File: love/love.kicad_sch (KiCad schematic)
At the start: 73 parts, among them U2 Raspberry_Pi_Pico

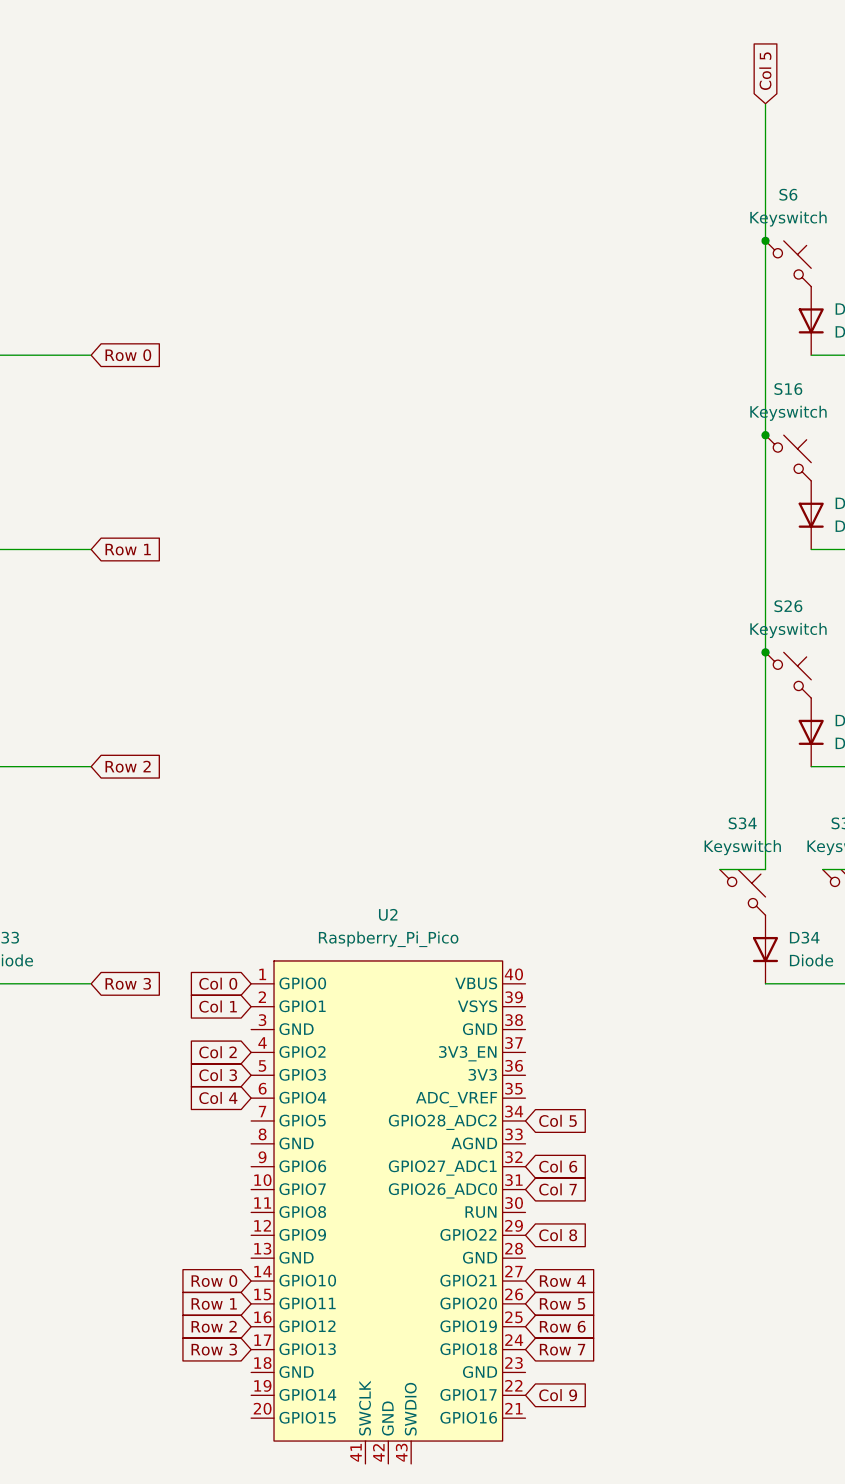
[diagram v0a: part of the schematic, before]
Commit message: adding the traditional 84 key but for somereason i named it 104
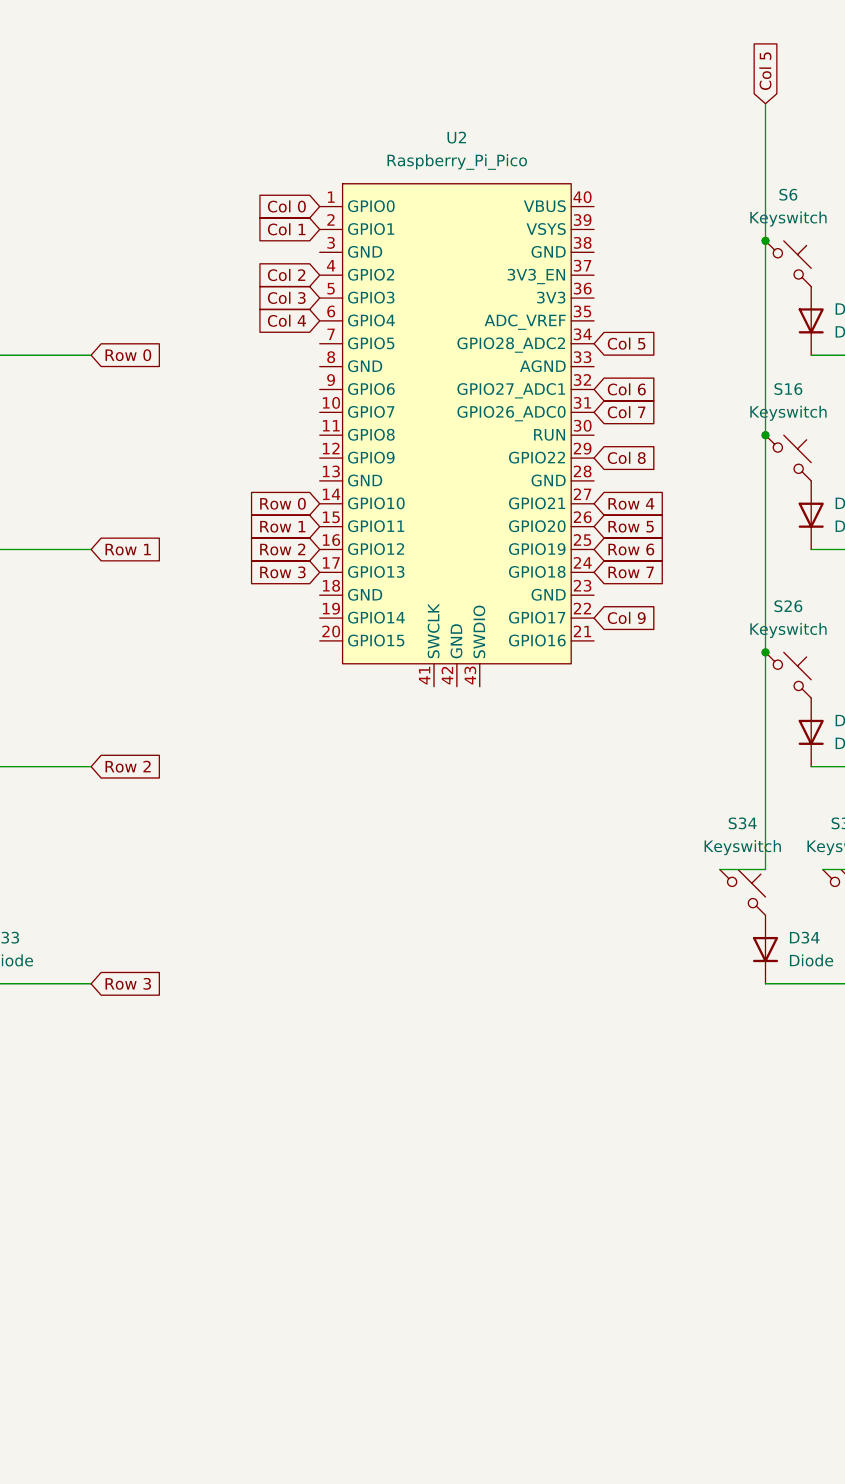
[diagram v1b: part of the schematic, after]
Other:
- moved on the sheet: U2
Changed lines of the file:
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@@
     (stroke (width 0) (type default))
   )
-  (global_label "Col 0" (shape input) (at 127 137.16 180) (fields_autoplaced)
+  (global_label "Col 0" (shape input) (at 134.62 50.8 180) (fields_autoplaced)
     (effects (font (size 1.27 1.27)) (justify right))
-    (property "Intersheetrefs" "${INTERSHEET_REFS}" (at 118.7535 137.16 0)
+    (property "Intersheetrefs" "${INTERSHEET_REFS}" (at 126.3735 50.8 0)
       (effects (font (size 1.27 1.27)) (justify right) hide)
     )
   )
-  (global_label "Col 4" (shape input) (at 127 149.86 180) (fields_autoplaced)
+  (global_label "Col 4" (shape input) (at 134.62 63.5 180) (fields_autoplaced)
     (effects (font (size 1.27 1.27)) (justify right))
-    (property "Intersheetrefs" "${INTERSHEET_REFS}" (at 118.7535 149.86 0)
+    (property "Intersheetrefs" "${INTERSHEET_REFS}" (at 126.3735 63.5 0)
       (effects (font (size 1.27 1.27)) (justify right) hide)
     )
@@
     )
   )
-  (global_label "Row 5" (shape input) (at 157.48 172.72 0) (fields_autoplaced)
-    (effects (font (size 1.27 1.27)) (justify left))
-    (property "Intersheetrefs" "${INTERSHEET_REFS}" (at 166.3918 172.72 0)
+  (global_label "Row 5" (shape input) (at 165.1 86.36 0) (fields_autoplaced)
+    (effects (font (size 1.27 1.27)) (justify left))
+    (property "Intersheetrefs" "${INTERSHEET_REFS}" (at 174.0118 86.36 0)
       (effects (font (size 1.27 1.27)) (justify left) hide)
     )
@@
     )
   )
-  (global_label "Col 7" (shape input) (at 157.48 160.02 0) (fields_autoplaced)
-    (effects (font (size 1.27 1.27)) (justify left))
-    (property "Intersheetrefs" "${INTERSHEET_REFS}" (at 165.7265 160.02 0)
+  (global_label "Col 7" (shape input) (at 165.1 73.66 0) (fields_autoplaced)
+    (effects (font (size 1.27 1.27)) (justify left))
+    (property "Intersheetrefs" "${INTERSHEET_REFS}" (at 173.3465 73.66 0)
       (effects (font (size 1.27 1.27)) (justify left) hide)
     )
@@
     )
   )
-  (global_label "Col 6" (shape input) (at 157.48 157.48 0) (fields_autoplaced)
-    (effects (font (size 1.27 1.27)) (justify left))
-    (property "Intersheetrefs" "${INTERSHEET_REFS}" (at 165.7265 157.48 0)
-      (effects (font (size 1.27 1.27)) (justify left) hide)
-    )
-  )
-  (global_label "Row 2" (shape input) (at 127 175.26 180) (fields_autoplaced)
+  (global_label "Col 6" (shape input) (at 165.1 71.12 0) (fields_autoplaced)
+    (effects (font (size 1.27 1.27)) (justify left))
+    (property "Intersheetrefs" "${INTERSHEET_REFS}" (at 173.3465 71.12 0)
+      (effects (font (size 1.27 1.27)) (justify left) hide)
+    )
+  )
+  (global_label "Row 2" (shape input) (at 134.62 88.9 180) (fields_autoplaced)
     (effects (font (size 1.27 1.27)) (justify right))
-    (property "Intersheetrefs" "${INTERSHEET_REFS}" (at 118.0882 175.26 0)
+    (property "Intersheetrefs" "${INTERSHEET_REFS}" (at 125.7082 88.9 0)
       (effects (font (size 1.27 1.27)) (justify right) hide)
     )
   )
-  (global_label "Row 3" (shape input) (at 127 177.8 180) (fields_autoplaced)
+  (global_label "Row 3" (shape input) (at 134.62 91.44 180) (fields_autoplaced)
     (effects (font (size 1.27 1.27)) (justify right))
-    (property "Intersheetrefs" "${INTERSHEET_REFS}" (at 118.0882 177.8 0)
+    (property "Intersheetrefs" "${INTERSHEET_REFS}" (at 125.7082 91.44 0)
       (effects (font (size 1.27 1.27)) (justify right) hide)
     )
@@
     )
   )
-  (global_label "Col 5" (shape input) (at 157.48 152.4 0) (fields_autoplaced)
-    (effects (font (size 1.27 1.27)) (justify left))
-    (property "Intersheetrefs" "${INTERSHEET_REFS}" (at 165.7265 152.4 0)
+  (global_label "Col 5" (shape input) (at 165.1 66.04 0) (fields_autoplaced)
+    (effects (font (size 1.27 1.27)) (justify left))
+    (property "Intersheetrefs" "${INTERSHEET_REFS}" (at 173.3465 66.04 0)
       (effects (font (size 1.27 1.27)) (justify left) hide)
     )
@@
     )
   )
-  (global_label "Col 9" (shape input) (at 157.48 182.88 0) (fields_autoplaced)
-    (effects (font (size 1.27 1.27)) (justify left))
-    (property "Intersheetrefs" "${INTERSHEET_REFS}" (at 165.7265 182.88 0)
-      (effects (font (size 1.27 1.27)) (justify left) hide)
-    )
-  )
-  (global_label "Col 3" (shape input) (at 127 147.32 180) (fields_autoplaced)
+  (global_label "Col 9" (shape input) (at 165.1 96.52 0) (fields_autoplaced)
+    (effects (font (size 1.27 1.27)) (justify left))
+    (property "Intersheetrefs" "${INTERSHEET_REFS}" (at 173.3465 96.52 0)
+      (effects (font (size 1.27 1.27)) (justify left) hide)
+    )
+  )
+  (global_label "Col 3" (shape input) (at 134.62 60.96 180) (fields_autoplaced)
     (effects (font (size 1.27 1.27)) (justify right))
-    (property "Intersheetrefs" "${INTERSHEET_REFS}" (at 118.7535 147.32 0)
+    (property "Intersheetrefs" "${INTERSHEET_REFS}" (at 126.3735 60.96 0)
       (effects (font (size 1.27 1.27)) (justify right) hide)
     )
@@
     )
   )
-  (global_label "Col 8" (shape input) (at 157.48 165.1 0) (fields_autoplaced)
-    (effects (font (size 1.27 1.27)) (justify left))
-    (property "Intersheetrefs" "${INTERSHEET_REFS}" (at 165.7265 165.1 0)
-      (effects (font (size 1.27 1.27)) (justify left) hide)
-    )
-  )
-  (global_label "Row 1" (shape input) (at 127 172.72 180) (fields_autoplaced)
+  (global_label "Col 8" (shape input) (at 165.1 78.74 0) (fields_autoplaced)
+    (effects (font (size 1.27 1.27)) (justify left))
+    (property "Intersheetrefs" "${INTERSHEET_REFS}" (at 173.3465 78.74 0)
+      (effects (font (size 1.27 1.27)) (justify left) hide)
+    )
+  )
+  (global_label "Row 1" (shape input) (at 134.62 86.36 180) (fields_autoplaced)
     (effects (font (size 1.27 1.27)) (justify right))
-    (property "Intersheetrefs" "${INTERSHEET_REFS}" (at 118.0882 172.72 0)
+    (property "Intersheetrefs" "${INTERSHEET_REFS}" (at 125.7082 86.36 0)
       (effects (font (size 1.27 1.27)) (justify right) hide)
     )
   )
-  (global_label "Row 4" (shape input) (at 157.48 170.18 0) (fields_autoplaced)
-    (effects (font (size 1.27 1.27)) (justify left))
-    (property "Intersheetrefs" "${INTERSHEET_REFS}" (at 166.3918 170.18 0)
+  (global_label "Row 4" (shape input) (at 165.1 83.82 0) (fields_autoplaced)
+    (effects (font (size 1.27 1.27)) (justify left))
+    (property "Intersheetrefs" "${INTERSHEET_REFS}" (at 174.0118 83.82 0)
       (effects (font (size 1.27 1.27)) (justify left) hide)
     )
@@
     )
   )
-  (global_label "Row 6" (shape input) (at 157.48 175.26 0) (fields_autoplaced)
-    (effects (font (size 1.27 1.27)) (justify left))
-    (property "Intersheetrefs" "${INTERSHEET_REFS}" (at 166.3918 175.26 0)
-      (effects (font (size 1.27 1.27)) (justify left) hide)
-    )
-  )
-  (global_label "Col 2" (shape input) (at 127 144.78 180) (fields_autoplaced)
+  (global_label "Row 6" (shape input) (at 165.1 88.9 0) (fields_autoplaced)
+    (effects (font (size 1.27 1.27)) (justify left))
+    (property "Intersheetrefs" "${INTERSHEET_REFS}" (at 174.0118 88.9 0)
+      (effects (font (size 1.27 1.27)) (justify left) hide)
+    )
+  )
+  (global_label "Col 2" (shape input) (at 134.62 58.42 180) (fields_autoplaced)
     (effects (font (size 1.27 1.27)) (justify right))
-    (property "Intersheetrefs" "${INTERSHEET_REFS}" (at 118.7535 144.78 0)
+    (property "Intersheetrefs" "${INTERSHEET_REFS}" (at 126.3735 58.42 0)
       (effects (font (size 1.27 1.27)) (justify right) hide)
     )
   )
-  (global_label "Row 0" (shape input) (at 127 170.18 180) (fields_autoplaced)
+  (global_label "Row 0" (shape input) (at 134.62 83.82 180) (fields_autoplaced)
     (effects (font (size 1.27 1.27)) (justify right))
-    (property "Intersheetrefs" "${INTERSHEET_REFS}" (at 118.0882 170.18 0)
+    (property "Intersheetrefs" "${INTERSHEET_REFS}" (at 125.7082 83.82 0)
       (effects (font (size 1.27 1.27)) (justify right) hide)
     )
   )
-  (global_label "Row 7" (shape input) (at 157.48 177.8 0) (fields_autoplaced)
-    (effects (font (size 1.27 1.27)) (justify left))
-    (property "Intersheetrefs" "${INTERSHEET_REFS}" (at 166.3918 177.8 0)
+  (global_label "Row 7" (shape input) (at 165.1 91.44 0) (fields_autoplaced)
+    (effects (font (size 1.27 1.27)) (justify left))
+    (property "Intersheetrefs" "${INTERSHEET_REFS}" (at 174.0118 91.44 0)
       (effects (font (size 1.27 1.27)) (justify left) hide)
     )
@@
     )
   )
-  (global_label "Col 1" (shape input) (at 127 139.7 180) (fields_autoplaced)
+  (global_label "Col 1" (shape input) (at 134.62 53.34 180) (fields_autoplaced)
     (effects (font (size 1.27 1.27)) (justify right))
-    (property "Intersheetrefs" "${INTERSHEET_REFS}" (at 118.7535 139.7 0)
+    (property "Intersheetrefs" "${INTERSHEET_REFS}" (at 126.3735 53.34 0)
       (effects (font (size 1.27 1.27)) (justify right) hide)
     )
@@
     )
   )
-  (symbol (lib_id "ScottoKeebs:MCU_Raspberry_Pi_Pico") (at 142.24 161.29 0) (unit 1)
-    (in_bom yes) (on_board yes) (dnp no) (fields_autoplaced)
-    (property "Reference" "U2" (at 142.24 129.54 0)
-      (effects (font (size 1.27 1.27)))
-    )
-    (property "Value" "Raspberry_Pi_Pico" (at 142.24 132.08 0)
-      (effects (font (size 1.27 1.27)))
-    )
-    (property "Footprint" "ScottoKeebs_MCU:Raspberry_Pi_Pico" (at 142.24 130.81 0)
-      (effects (font (size 1.27 1.27)) hide)
-    )
-    (property "Datasheet" "" (at 142.24 161.29 0)
-      (effects (font (size 1.27 1.27)) hide)
-    )
+  (symbol (lib_id "ScottoKeebs:MCU_Raspberry_Pi_Pico") (at 149.86 74.93 0) (unit 1)
+    (in_bom yes) (on_board yes) (dnp no) (fields_autoplaced)
+    (property "Reference" "U2" (at 149.86 43.18 0)
+      (effects (font (size 1.27 1.27)))
+    )
+    (property "Value" "Raspberry_Pi_Pico" (at 149.86 45.72 0)
+      (effects (font (size 1.27 1.27)))
+    )
+    (property "Footprint" "ScottoKeebs_MCU:Raspberry_Pi_Pico" (at 149.86 44.45 0)
+      (effects (font (size 1.27 1.27)) hide)
+    )
+    (property "Datasheet" "" (at 149.86 74.93 0)
+      (effects (font (size 1.27 1.27)) hide)
+    )
